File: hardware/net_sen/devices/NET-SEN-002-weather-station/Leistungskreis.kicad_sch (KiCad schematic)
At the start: 7 parts, among them J5 Input_x3

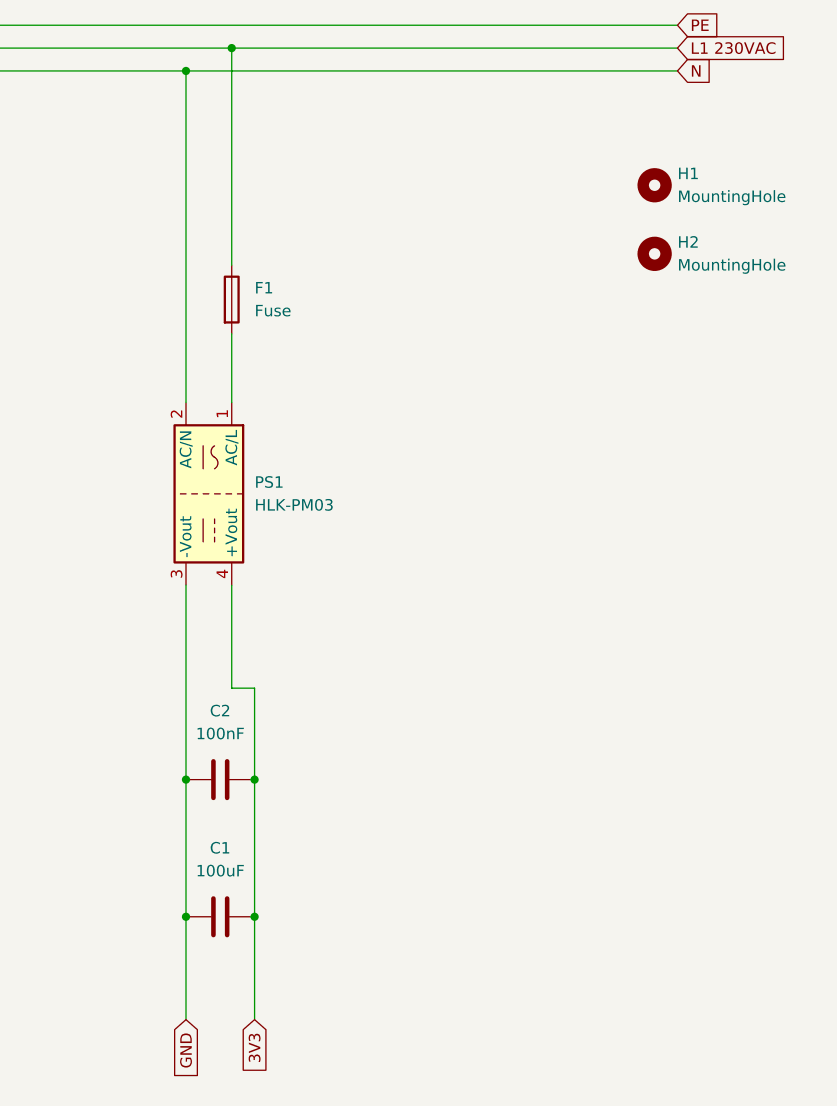
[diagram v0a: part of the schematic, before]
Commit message: öffentliche Präsentation bereinigt: KI-Referenzen entfernt, READMEs optimiert, Firmware als Hauptlinie, ESPHome als Alternative mit Disclaimer
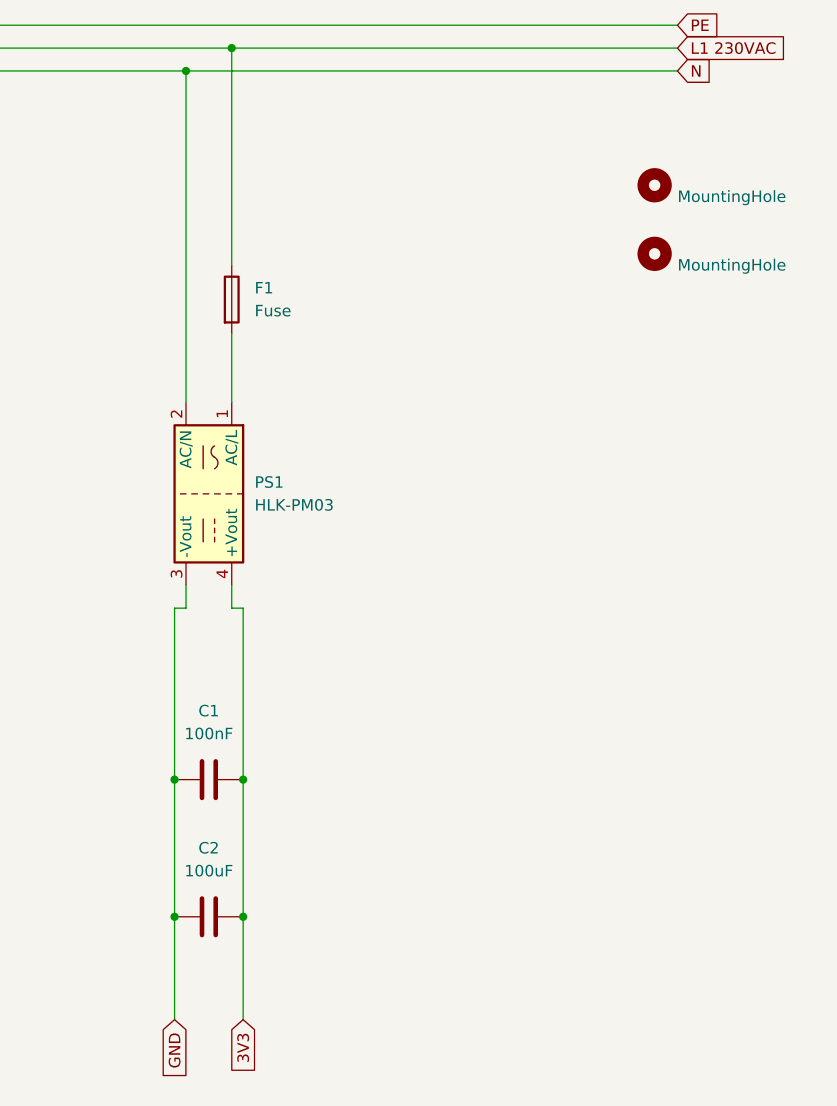
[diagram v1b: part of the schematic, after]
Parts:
- renumbered C2 to C1, C1 to C2
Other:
- title: (none) -> Leistungskreis
- moved on the sheet: C1, C2
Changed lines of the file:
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@@
 	(generator_version "9.0")
 	(paper "A4")
+	(title_block
+		(title "Leistungskreis")
+		(date "2026-05-30")
+		(comment 1 "HLK-PM03 Netzteil 230V -> 3.3V")
+	)
 	(junction
-		(at 222.25 100.33)
+		(at 213.36 100.33)
+		(diameter 0)
+		(color 0 0 0 0)
+	)
+	(junction
+		(at 220.98 100.33)
 		(diameter 0)
 		(color 0 0 0 0)
@@
 	)
 	(junction
+		(at 220.98 115.57)
+		(diameter 0)
+		(color 0 0 0 0)
+	)
+	(junction
 		(at 219.71 19.05)
 		(diameter 0)
@@
 	)
 	(junction
-		(at 214.63 100.33)
+		(at 213.36 115.57)
 		(diameter 0)
 		(color 0 0 0 0)
 	)
-	(junction
-		(at 222.25 115.57)
-		(diameter 0)
-		(color 0 0 0 0)
-	)
-	(junction
-		(at 214.63 115.57)
-		(diameter 0)
-		(color 0 0 0 0)
-	)
 	(wire
 		(pts
@@
 	(wire
 		(pts
-			(xy 222.25 90.17) (xy 222.25 100.33)
-		)
-		(stroke
-			(width 0)
-			(type default)
-		)
-	)
-	(wire
-		(pts
-			(xy 219.71 90.17) (xy 222.25 90.17)
-		)
-		(stroke
-			(width 0)
-			(type default)
-		)
-	)
-	(wire
-		(pts
-			(xy 214.63 100.33) (xy 214.63 115.57)
-		)
-		(stroke
-			(width 0)
-			(type default)
-		)
-	)
-	(wire
-		(pts
-			(xy 219.71 78.74) (xy 219.71 90.17)
+			(xy 220.98 81.28) (xy 220.98 100.33)
+		)
+		(stroke
+			(width 0)
+			(type default)
+		)
+	)
+	(wire
+		(pts
+			(xy 219.71 81.28) (xy 220.98 81.28)
+		)
+		(stroke
+			(width 0)
+			(type default)
+		)
+	)
+	(wire
+		(pts
+			(xy 213.36 115.57) (xy 213.36 127)
 		)
 		(stroke
@@
 	(wire
 		(pts
+			(xy 213.36 100.33) (xy 213.36 115.57)
+		)
+		(stroke
+			(width 0)
+			(type default)
+		)
+	)
+	(wire
+		(pts
+			(xy 214.63 78.74) (xy 214.63 81.28)
+		)
+		(stroke
+			(width 0)
+			(type default)
+		)
+	)
+	(wire
+		(pts
 			(xy 219.71 19.05) (xy 269.24 19.05)
 		)
@@
 	(wire
 		(pts
-			(xy 222.25 115.57) (xy 222.25 127)
-		)
-		(stroke
-			(width 0)
-			(type default)
-		)
-	)
-	(wire
-		(pts
-			(xy 214.63 115.57) (xy 214.63 127)
-		)
-		(stroke
-			(width 0)
-			(type default)
-		)
-	)
-	(wire
-		(pts
-			(xy 222.25 100.33) (xy 222.25 115.57)
-		)
-		(stroke
-			(width 0)
-			(type default)
-		)
-	)
-	(wire
-		(pts
-			(xy 214.63 78.74) (xy 214.63 100.33)
+			(xy 220.98 115.57) (xy 220.98 127)
+		)
+		(stroke
+			(width 0)
+			(type default)
+		)
+	)
+	(wire
+		(pts
+			(xy 214.63 81.28) (xy 213.36 81.28)
+		)
+		(stroke
+			(width 0)
+			(type default)
+		)
+	)
+	(wire
+		(pts
+			(xy 213.36 81.28) (xy 213.36 100.33)
 		)
 		(stroke
@@
 	(wire
 		(pts
+			(xy 219.71 78.74) (xy 219.71 81.28)
+		)
+		(stroke
+			(width 0)
+			(type default)
+		)
+	)
+	(wire
+		(pts
 			(xy 22.86 16.51) (xy 269.24 16.51)
+		)
+		(stroke
+			(width 0)
+			(type default)
+		)
+	)
+	(wire
+		(pts
+			(xy 220.98 100.33) (xy 220.98 115.57)
 		)
 		(stroke
@@
 	(global_label "3V3"
 		(shape input)
-		(at 222.25 127 270)
+		(at 220.98 127 270)
 		(fields_autoplaced yes)
 		(effects
@@
 		)
 		(property "Intersheetrefs" "${INTERSHEET_REFS}"
-			(at 222.25 133.4928 90)
+			(at 220.98 133.4928 90)
 			(effects
 				(font
@@
 	(global_label "GND"
 		(shape input)
-		(at 214.63 127 270)
+		(at 213.36 127 270)
 		(fields_autoplaced yes)
 		(effects
@@
 		)
 		(property "Intersheetrefs" "${INTERSHEET_REFS}"
-			(at 214.63 133.8557 90)
+			(at 213.36 133.8557 90)
 			(effects
 				(font
@@
 		(dnp no)
 		(fields_autoplaced yes)
-		(property "Reference" "H1"
+		(property "Reference" "H?"
 			(at 269.24 33.0199 0)
 			(effects
@@
 				)
 				(justify left)
+				(hide yes)
 			)
 		)
@@
 				(path "/10108191-213d-452b-b5d4-aff556accf72/25d7b4fa-577d-4dec-b1c0-3ffdf80ff8a0"
 					(reference "H1")
+					(unit 1)
+				)
+			)
+			(project "Leistungskreis"
+				(path "/10336860-6b83-4ee6-b068-87976d7f0c35"
+					(reference "H?")
 					(unit 1)
 				)
@@
 		(on_board yes)
 		(dnp no)
-		(property "Reference" "J5"
+		(property "Reference" "J?"
 			(at 10.922 19.05 0)
 			(effects
@@
 				)
 			)
+			(project "Leistungskreis"
+				(path "/10336860-6b83-4ee6-b068-87976d7f0c35"
+					(reference "J?")
+					(unit 1)
+				)
+			)
 		)
 	)
 	(symbol
 		(lib_id "Device:C")
-		(at 218.44 100.33 90)
+		(at 217.17 100.33 90)
 		(unit 1)
 		(exclude_from_sim no)
@@
 		(dnp no)
 		(fields_autoplaced yes)
-		(property "Reference" "C2"
-			(at 218.44 92.71 90)
+		(property "Reference" "C1"
+			(at 217.17 92.71 90)
 			(effects
 				(font
@@
 		)
 		(property "Value" "100nF"
-			(at 218.44 95.25 90)
+			(at 217.17 95.25 90)
 			(effects
 				(font
@@
 		)
 		(property "Footprint" "Capacitor_SMD:C_0805_2012Metric_Pad1.18x1.45mm_HandSolder"
-			(at 222.25 99.3648 0)
+			(at 220.98 99.3648 0)
 			(effects
 				(font
@@
 		)
 		(property "Datasheet" "~"
-			(at 218.44 100.33 0)
+			(at 217.17 100.33 0)
 			(effects
 				(font
@@
 		)
 		(property "Description" "Unpolarized capacitor"
-			(at 218.44 100.33 0)
+			(at 217.17 100.33 0)
 			(effects
 				(font
@@
 				(path "/10108191-213d-452b-b5d4-aff556accf72/25d7b4fa-577d-4dec-b1c0-3ffdf80ff8a0"
 					(reference "C2")
+					(unit 1)
+				)
+			)
+			(project "Leistungskreis"
+				(path "/10336860-6b83-4ee6-b068-87976d7f0c35"
+					(reference "C1")
 					(unit 1)
 				)
@@
 		(dnp no)
 		(fields_autoplaced yes)
-		(property "Reference" "H2"
+		(property "Reference" "H?"
 			(at 269.24 40.6399 0)
 			(effects
@@
 				)
 				(justify left)
+				(hide yes)
 			)
 		)
@@
 				)
 			)
+			(project "Leistungskreis"
+				(path "/10336860-6b83-4ee6-b068-87976d7f0c35"
+					(reference "H?")
+					(unit 1)
+				)
+			)
 		)
 	)
 	(symbol
 		(lib_id "Device:C")
-		(at 218.44 115.57 270)
+		(at 217.17 115.57 270)
 		(unit 1)
 		(exclude_from_sim no)
@@
 		(dnp no)
 		(fields_autoplaced yes)
-		(property "Reference" "C1"
-			(at 218.44 107.95 90)
+		(property "Reference" "C2"
+			(at 217.17 107.95 90)
 			(effects
 				(font
@@
 		)
 		(property "Value" "100uF"
-			(at 218.44 110.49 90)
+			(at 217.17 110.49 90)
 			(effects
 				(font
@@
 		)
 		(property "Footprint" "Capacitor_SMD:CP_Elec_6.3x5.8"
-			(at 214.63 116.5352 0)
+			(at 213.36 116.5352 0)
 			(effects
 				(font
@@
 		)
 		(property "Datasheet" "~"
-			(at 218.44 115.57 0)
+			(at 217.17 115.57 0)
 			(effects
 				(font
@@
 		)
 		(property "Description" "Unpolarized capacitor"
-			(at 218.44 115.57 0)
+			(at 217.17 115.57 0)
 			(effects
 				(font
@@
 				(path "/10108191-213d-452b-b5d4-aff556accf72/25d7b4fa-577d-4dec-b1c0-3ffdf80ff8a0"
 					(reference "C1")
+					(unit 1)
+				)
+			)
+			(project "Leistungskreis"
+				(path "/10336860-6b83-4ee6-b068-87976d7f0c35"
+					(reference "C2")
 					(unit 1)
 				)
@@
 				)
 			)
+			(project "Leistungskreis"
+				(path "/10336860-6b83-4ee6-b068-87976d7f0c35"
+					(reference "PS1")
+					(unit 1)
+				)
+			)
 		)
 	)
@@
 				)
 			)
-		)
-	)
+			(project "Leistungskreis"
+				(path "/10336860-6b83-4ee6-b068-87976d7f0c35"
+					(reference "F1")
+					(unit 1)
+				)
+			)
+		)
+	)
+	(sheet_instances
+		(path "/"
+			(page "1")
+		)
+	)
+	(embedded_fonts no)
 )
